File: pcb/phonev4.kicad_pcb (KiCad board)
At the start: 2 copper layers, 88.9 x 124.5 mm, 25 parts, among them J1 coin, J2 keypad, J3 display, J4 RJ9, J5 mic, J6 card_reader, J7 speaker, U2 LM386

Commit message: pcb: Rename power nets 5v→5V_MAIN, 12v→12V_COIN (fixes #69)
- Schematic: global_label and TP1 Value
- PCB: net definitions, pads, pour zone net_name

Co-authored-by: Cursor <cursoragent@cursor.com>
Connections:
- net 12v renamed 12V_COIN
- net 5v renamed 5V_MAIN
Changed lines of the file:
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@@
   (net 0 "")
   (net 1 "unconnected-(A1-3.3V-Pad3V3)")
-  (net 2 "5v")
+  (net 2 "5V_MAIN")
   (net 3 "mag_cls")
   (net 4 "unconnected-(A1-PadAREF)")
@@
   (net 86 "unconnected-(J3-Pin_24-Pad24)")
   (net 87 "gnd")
-  (net 88 "12v")
+  (net 88 "12V_COIN")
   (net 89 "coin_tx")
   (net 90 "coin_rx")
@@
       (net 107 "Net-(C3-Pad1)") (pintype "output") (solder_mask_margin 0.102))
     (pad "6" thru_hole circle (at 1.27 -3.81) (size 1.7272 1.7272) (drill 0.8128) (layers "*.Cu" "*.Mask")
-      (net 88 "12v") (pinfunction "V+") (pintype "power_in") (solder_mask_margin 0.102))
+      (net 88 "12V_COIN") (pinfunction "V+") (pintype "power_in") (solder_mask_margin 0.102))
     (pad "7" thru_hole circle (at -1.27 -3.81) (size 1.7272 1.7272) (drill 0.8128) (layers "*.Cu" "*.Mask")
       (net 106 "Net-(U2-BYPASS)") (pinfunction "BYPASS") (pintype "input") (solder_mask_margin 0.102))
@@
       (net 29 "disp_d7") (pinfunction "Pin_1") (pintype "passive"))
     (pad "2" thru_hole circle (at 2.54 0 90) (size 1.7 1.7) (drill 1) (layers "*.Cu" "*.Mask")
-      (net 2 "5v") (pinfunction "Pin_2") (pintype "passive"))
+      (net 2 "5V_MAIN") (pinfunction "Pin_2") (pintype "passive"))
     (pad "3" thru_hole circle (at 0 2.54 90) (size 1.7 1.7) (drill 1) (layers "*.Cu" "*.Mask")
       (net 28 "disp_d6") (pinfunction "Pin_3") (pintype "passive"))
@@
       (net 87 "gnd") (pinfunction "Pin_8") (pintype "passive"))
     (pad "9" thru_hole circle (at 0 10.16 90) (size 1.7 1.7) (drill 1) (layers "*.Cu" "*.Mask")
-      (net 88 "12v") (pinfunction "Pin_9") (pintype "passive"))
+      (net 88 "12V_COIN") (pinfunction "Pin_9") (pintype "passive"))
     (pad "10" thru_hole circle (at 2.54 10.16 90) (size 1.7 1.7) (drill 1) (layers "*.Cu" "*.Mask")
       (net 91 "coin_reset") (pinfunction "Pin_10") (pintype "passive"))
@@
       (stroke (width 0.1) (type solid)) (layer "F.Fab"))
     (pad "1" thru_hole circle (at 0 0 90) (size 1.6 1.6) (drill 0.8) (layers "*.Cu" "*.Mask")
-      (net 2 "5v") (pintype "passive"))
+      (net 2 "5V_MAIN") (pintype "passive"))
     (pad "2" thru_hole oval (at 7.5 0 90) (size 1.6 1.6) (drill 0.8) (layers "*.Cu" "*.Mask")
       (net 87 "gnd") (pintype "passive"))
@@
       (net 87 "gnd") (pintype "passive"))
     (pad "2" thru_hole oval (at 7.5 0 270) (size 1.6 1.6) (drill 0.8) (layers "*.Cu" "*.Mask")
-      (net 2 "5v") (pintype "passive"))
+      (net 2 "5V_MAIN") (pintype "passive"))
     (model "${KICAD6_3DMODEL_DIR}/Capacitor_THT.3dshapes/C_Axial_L3.8mm_D2.6mm_P7.50mm_Horizontal.wrl"
       (offset (xyz 0 0 0))
@@
       (stroke (width 0.1) (type solid)) (layer "F.Fab"))
     (pad "1" thru_hole circle (at 0 0 180) (size 1.6 1.6) (drill 0.8) (layers "*.Cu" "*.Mask")
-      (net 2 "5v") (pintype "passive"))
+      (net 2 "5V_MAIN") (pintype "passive"))
     (pad "2" thru_hole oval (at 7.5 0 180) (size 1.6 1.6) (drill 0.8) (layers "*.Cu" "*.Mask")
       (net 87 "gnd") (pintype "passive"))
@@
       (stroke (width 0.1) (type solid)) (layer "F.Fab"))
     (pad "1" thru_hole circle (at 0 0 90) (size 1.6 1.6) (drill 0.8) (layers "*.Cu" "*.Mask")
-      (net 88 "12v") (pintype "passive"))
+      (net 88 "12V_COIN") (pintype "passive"))
     (pad "2" thru_hole oval (at 7.5 0 90) (size 1.6 1.6) (drill 0.8) (layers "*.Cu" "*.Mask")
       (net 87 "gnd") (pintype "passive"))
@@
       (net 33 "unconnected-(A3-3V3[1]-Pad1)") (pinfunction "3V3[1]") (pintype "power_in") (solder_mask_margin 0.102))
     (pad "2" thru_hole circle (at -24.13 -1.27 90) (size 1.508 1.508) (drill 1) (layers "*.Cu" "*.Mask")
-      (net 2 "5v") (pinfunction "5V[1]") (pintype "power_in") (solder_mask_margin 0.102))
+      (net 2 "5V_MAIN") (pinfunction "5V[1]") (pintype "power_in") (solder_mask_margin 0.102))
     (pad "3" thru_hole circle (at -21.59 1.27 90) (size 1.508 1.508) (drill 1) (layers "*.Cu" "*.Mask")
       (net 34 "unconnected-(A3-GPIO2{slash}SDA-Pad3)") (pinfunction "GPIO2/SDA") (pintype "bidirectional") (solder_mask_margin 0.102))
     (pad "4" thru_hole circle (at -21.59 -1.27 90) (size 1.508 1.508) (drill 1) (layers "*.Cu" "*.Mask")
-      (net 2 "5v") (pinfunction "5V[2]") (pintype "power_in") (solder_mask_margin 0.102))
+      (net 2 "5V_MAIN") (pinfunction "5V[2]") (pintype "power_in") (solder_mask_margin 0.102))
     (pad "5" thru_hole circle (at -19.05 1.27 90) (size 1.508 1.508) (drill 1) (layers "*.Cu" "*.Mask")
       (net 35 "unconnected-(A3-GPIO3{slash}SCL-Pad5)") (pinfunction "GPIO3/SCL") (pintype "bidirectional") (solder_mask_margin 0.102))
@@
       (net 1 "unconnected-(A1-3.3V-Pad3V3)") (pinfunction "3.3V") (pintype "power_out"))
     (pad "5V" thru_hole oval (at 31.86 -1.38) (size 1.7272 1.7272) (drill 1.016) (layers "*.Cu" "*.Mask")
-      (net 2 "5v") (pinfunction "5V") (pintype "power_in"))
+      (net 2 "5V_MAIN") (pinfunction "5V") (pintype "power_in"))
     (pad "A0" thru_hole oval (at 11.54 -1.38) (size 1.7272 1.7272) (drill 1.016) (layers "*.Cu" "*.Mask")
       (net 93 "key_col_5") (pinfunction "A0") (pintype "bidirectional"))
@@
       (net 12 "ss") (pinfunction "SPI_CS") (pintype "bidirectional"))
     (pad "VIN" thru_hole oval (at 39.48 -1.38) (size 1.7272 1.7272) (drill 1.016) (layers "*.Cu" "*.Mask")
-      (net 2 "5v") (pinfunction "VIN") (pintype "power_in"))
+      (net 2 "5V_MAIN") (pinfunction "VIN") (pintype "power_in"))
   )
   (footprint "Connector_IDC:IDC-Header_2x07_P2.54mm_Vertical" (layer "F.Cu")
@@
       (net 73 "unconnected-(J6-Pin_10-Pad10)") (pinfunction "Pin_10") (pintype "passive"))
     (pad "11" thru_hole circle (at 0 12.7 90) (size 1.7 1.7) (drill 1) (layers "*.Cu" "*.Mask")
-      (net 2 "5v") (pinfunction "Pin_11") (pintype "passive"))
+      (net 2 "5V_MAIN") (pinfunction "Pin_11") (pintype "passive"))
     (pad "12" thru_hole circle (at 2.54 12.7 90) (size 1.7 1.7) (drill 1) (layers "*.Cu" "*.Mask")
       (net 61 "card_seated") (pinfunction "Pin_12") (pintype "passive"))
@@
       (net 13 "unconnected-(A2-3.3V-Pad3V3)") (pinfunction "3.3V") (pintype "power_out"))
     (pad "5V" thru_hole oval (at 31.86 -1.38) (size 1.7272 1.7272) (drill 1.016) (layers "*.Cu" "*.Mask")
-      (net 2 "5v") (pinfunction "5V") (pintype "power_in"))
+      (net 2 "5V_MAIN") (pinfunction "5V") (pintype "power_in"))
     (pad "A0" thru_hole oval (at 11.54 -1.38) (size 1.7272 1.7272) (drill 1.016) (layers "*.Cu" "*.Mask")
       (net 110 "unconnected-(A2-PadA0)") (pinfunction "A0") (pintype "bidirectional"))
@@
       (net 17 "disp_x4") (pinfunction "SPI_CS") (pintype "bidirectional"))
     (pad "VIN" thru_hole oval (at 39.48 -1.38) (size 1.7272 1.7272) (drill 1.016) (layers "*.Cu" "*.Mask")
-      (net 2 "5v") (pinfunction "VIN") (pintype "power_in"))
+      (net 2 "5V_MAIN") (pinfunction "VIN") (pintype "power_in"))
   )
   (footprint "Resistor_THT:R_Axial_DIN0204_L3.6mm_D1.6mm_P7.62mm_Horizontal" (layer "F.Cu")
@@
       (stroke (width 0.1) (type solid)) (layer "F.Fab"))
     (pad "1" thru_hole circle (at 0 0 270) (size 1.4 1.4) (drill 0.7) (layers "*.Cu" "*.Mask")
-      (net 2 "5v") (pintype "passive"))
+      (net 2 "5V_MAIN") (pintype "passive"))
     (pad "2" thru_hole oval (at 7.62 0 270) (size 1.4 1.4) (drill 0.7) (layers "*.Cu" "*.Mask")
       (net 19 "sda") (pintype "passive"))
@@
       (stroke (width 0.1) (type solid)) (layer "F.Fab"))
     (pad "1" thru_hole circle (at 0 0 270) (size 1.4 1.4) (drill 0.7) (layers "*.Cu" "*.Mask")
-      (net 2 "5v") (pintype "passive"))
+      (net 2 "5V_MAIN") (pintype "passive"))
     (pad "2" thru_hole oval (at 7.62 0 270) (size 1.4 1.4) (drill 0.7) (layers "*.Cu" "*.Mask")
       (net 20 "scl") (pintype "passive"))
@@
       (stroke (width 0.1) (type solid)) (layer "F.Fab"))
     (pad "1" thru_hole circle (at 0 0 180) (size 1.6 1.6) (drill 0.8) (layers "*.Cu" "*.Mask")
-      (net 2 "5v") (pintype "passive"))
+      (net 2 "5V_MAIN") (pintype "passive"))
     (pad "2" thru_hole oval (at 7.5 0 180) (size 1.6 1.6) (drill 0.8) (layers "*.Cu" "*.Mask")
       (net 87 "gnd") (pintype "passive"))
@@
       (stroke (width 0.15) (type solid)) (fill none) (layer "F.SilkS"))
     (pad "1" thru_hole rect (at -41.3258 -19.1516 90) (size 1.524 1.524) (drill 1) (layers "*.Cu" "*.Mask" "F.SilkS")
-      (net 2 "5v") (pinfunction "IN+") (pintype "input"))
+      (net 2 "5V_MAIN") (pinfunction "IN+") (pintype "input"))
     (pad "2" thru_hole rect (at -41.3258 -1.9812 90) (size 1.524 1.524) (drill 1) (layers "*.Cu" "*.Mask" "F.SilkS")
       (net 87 "gnd") (pinfunction "IN-") (pintype "input"))
@@
       (net 87 "gnd") (pinfunction "OUT-") (pintype "output"))
     (pad "4" thru_hole rect (at -1.8542 -19.1262 90) (size 1.524 1.524) (drill 1) (layers "*.Cu" "*.Mask" "F.SilkS")
-      (net 88 "12v") (pinfunction "OUT+") (pintype "output"))
+      (net 88 "12V_COIN") (pinfunction "OUT+") (pintype "output"))
   )
   (footprint "Capacitor_THT:CP_Radial_D8.0mm_P3.80mm" (layer "F.Cu")
@@
       (stroke (width 0.1) (type solid)) (fill none) (layer "F.Fab"))
     (pad "1" thru_hole rect (at 0 0) (size 1.6 1.6) (drill 0.8) (layers "*.Cu" "*.Mask")
-      (net 88 "12v") (pintype "passive"))
+      (net 88 "12V_COIN") (pintype "passive"))
     (pad "2" thru_hole circle (at 3.8 0) (size 1.6 1.6) (drill 0.8) (layers "*.Cu" "*.Mask")
       (net 87 "gnd") (pintype "passive"))
@@
     )
   )
-  (zone (net 2) (net_name "5v") (layer "B.Cu") (hatch edge 0.5)
+  (zone (net 2) (net_name "5V_MAIN") (layer "B.Cu") (hatch edge 0.5)
     (priority 1)
     (connect_pads (clearance 0.5))

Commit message: pcb: Move D2 ESD protection from coin_rx to speaker_front+
- D2 (PRTR5V0U2X) now protects speaker_front+ (TDA2822 ringer output)
  instead of coin_rx; coin validator control board isolates serial
- D1 protects mic+ and speaker_receiver+ on J4; D2 I/O2 left unconnected
- Add SCHEMATIC_D2_CHANGES.md with implementation notes and I/O2 options
- Update README, BOM, AUDIT to match

Co-authored-by: Cursor <cursoragent@cursor.com>
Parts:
- added C10: 100nF, Capacitor_THT:C_Axial_L3.8mm_D2.6mm_P7.50mm_Horizontal, F.Cu at (79.6, 55.1)
- added C11: 100µF 16V, Capacitor_THT:CP_Radial_D8.0mm_P3.80mm, F.Cu at (71.4, 49.5)
- added C6: 100nF, Capacitor_THT:C_Axial_L3.8mm_D2.6mm_P7.50mm_Horizontal, F.Cu at (79.6, 46.8)
- added C7: 100µF 16V, Capacitor_THT:CP_Radial_D8.0mm_P3.80mm, F.Cu at (71.4, 59.0)
- added C8: 4.7µF, Capacitor_THT:CP_Radial_D5.0mm_P2.00mm, F.Cu at (91.0, 72.0)
- added C9: 100nF, Capacitor_THT:C_Axial_L3.8mm_D2.6mm_P7.50mm_Horizontal, F.Cu at (79.6, 51.0)
- added D1: PRTR5V0U2X, Package_TO_SOT_SMD:SOT-143, F.Cu at (70.5, 66.2)
- added D2: PRTR5V0U2X, Package_TO_SOT_SMD:SOT-143, F.Cu at (74.7, 66.2)
- added D3: Green LED, LED_THT:LED_D5.0mm, F.Cu at (70.8, 72.2)
- added F1: 1A, Capacitor_THT:CP_Radial_D10.0mm_P5.00mm, F.Cu at (81.6, 63.0)
- added Q1: Si2319CDS, Package_TO_SOT_SMD:SOT-23, F.Cu at (92.3, 59.4)
- added R3: 1kΩ, Resistor_THT:R_Axial_DIN0204_L3.6mm_D1.6mm_P7.62mm_Horizontal, F.Cu at (79.5, 70.3)
- added TP1: 5V_MAIN, TestPoint:TestPoint_Loop_D2.50mm_Drill1.0mm, F.Cu at (66.0, 47.0)
- added TP2: Pi 3.3v out, TestPoint:TestPoint_Loop_D2.50mm_Drill1.0mm, F.Cu at (66.0, 51.7)
- added TP3: Ground, TestPoint:TestPoint_Loop_D2.50mm_Drill1.0mm, F.Cu at (66.0, 56.4)
- added TP4: SDA, TestPoint:TestPoint_Loop_D2.50mm_Drill1.0mm, F.Cu at (66.0, 61.0)
- added TP5: SCL, TestPoint:TestPoint_Loop_D2.50mm_Drill1.0mm, F.Cu at (66.0, 65.7)
- C12: renamed from C3; value CP_Axial_L18.0mm_D10.0mm_P25.00mm -> 100µF 16V; footprint Capacitor_THT:CP_Radial_D10.0mm_P3.80mm -> Capacitor_THT:CP_Radial_D8.0mm_P3.80mm
- R1, R2: value 10k -> 4.7k
- U2: value LM386 -> TDA2822M; footprint LM386:DIP08 -> Package_DIP:DIP-8_W7.62mm
- renumbered C-arduino1 to C1, C-arduino-display1 to C2, C-card1 to C3, C-coin1 to C4, C-raspi1 to C5
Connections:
- A1 pad GND1: gnd -> GND
- A1 pad GND2: gnd -> GND
- A2 pad GND1: gnd -> GND
- A2 pad GND2: gnd -> GND
- A3 pad 1: unconnected-(A3-3V3[1]-Pad1) -> Net-(A3-3V3[1])
- A3 pad 14: gnd -> GND
- A3 pad 20: gnd -> GND
- A3 pad 25: gnd -> GND
- A3 pad 30: gnd -> GND
- A3 pad 34: gnd -> GND
- A3 pad 39: gnd -> GND
- A3 pad 6: gnd -> GND
- A3 pad 9: gnd -> GND
- C1 pad 2: gnd -> GND
- C12 pad 2: speaker_front+ -> speaker_receiver+
- C2 pad 2: gnd -> GND
- C3 pad 1: gnd -> GND
- C4 pad 2: gnd -> GND
- C5 pad 2: gnd -> GND
- J1 pad 1: gnd -> GND
- J1 pad 4: gnd -> GND
- J1 pad 5: gnd -> GND
- J1 pad 6: gnd -> GND
- J1 pad 7: gnd -> GND
- J1 pad 8: gnd -> GND
- J2 pad 20: gnd -> GND
- J3 pad 26: gnd -> GND
- J4 pad 3: gnd -> GND
- J4 pad 4: gnd -> GND
- J5 pad 2: gnd -> GND
- J6 pad 12: card_seated -> mag_cls
- J6 pad 2: gnd -> GND
- J7 pad 1: speaker_receiver+ -> speaker_receiver_pre+
- J7 pad 2: gnd -> GND
- U1 pad 1: 5V_MAIN -> BOOST_IN+
- U1 pad 2: gnd -> GND
- U1 pad 3: gnd -> GND
- U2 pad 1: unconnected-(U2-GAIN-Pad1) -> Net-(U2-OUT_A)
- U2 pad 2: gnd -> GND
- U2 pad 3: speaker_front_pre+ -> Net-(U2-IN_A)
- U2 pad 4: gnd -> Net-(U2-IN_B)
- U2 pad 6: 12V_COIN -> 5V_MAIN
- U2 pad 7: Net-(U2-BYPASS) -> Net-(U2-RIPPLE)
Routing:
- net 12V_COIN: track 170.7 -> 38.7 mm
- net speaker_front+: track 118.6 -> 0.00 mm
- net gnd: track 111.4 -> 0.00 mm, vias 2 -> 0
- net GND: track 0.00 -> 95.4 mm, vias 0 -> 2
- net speaker_front_pre+: track 48.1 -> 0.00 mm
- net Net-(U2-OUT_B): track 23.7 -> 0.00 mm
- net speaker_receiver+: track 19.6 -> 0.00 mm
- net Net-(U2-BYPASS): track 16.1 -> 0.00 mm
- added copper zone on F.Cu, net GND
- removed copper zone on F.Cu, net gnd

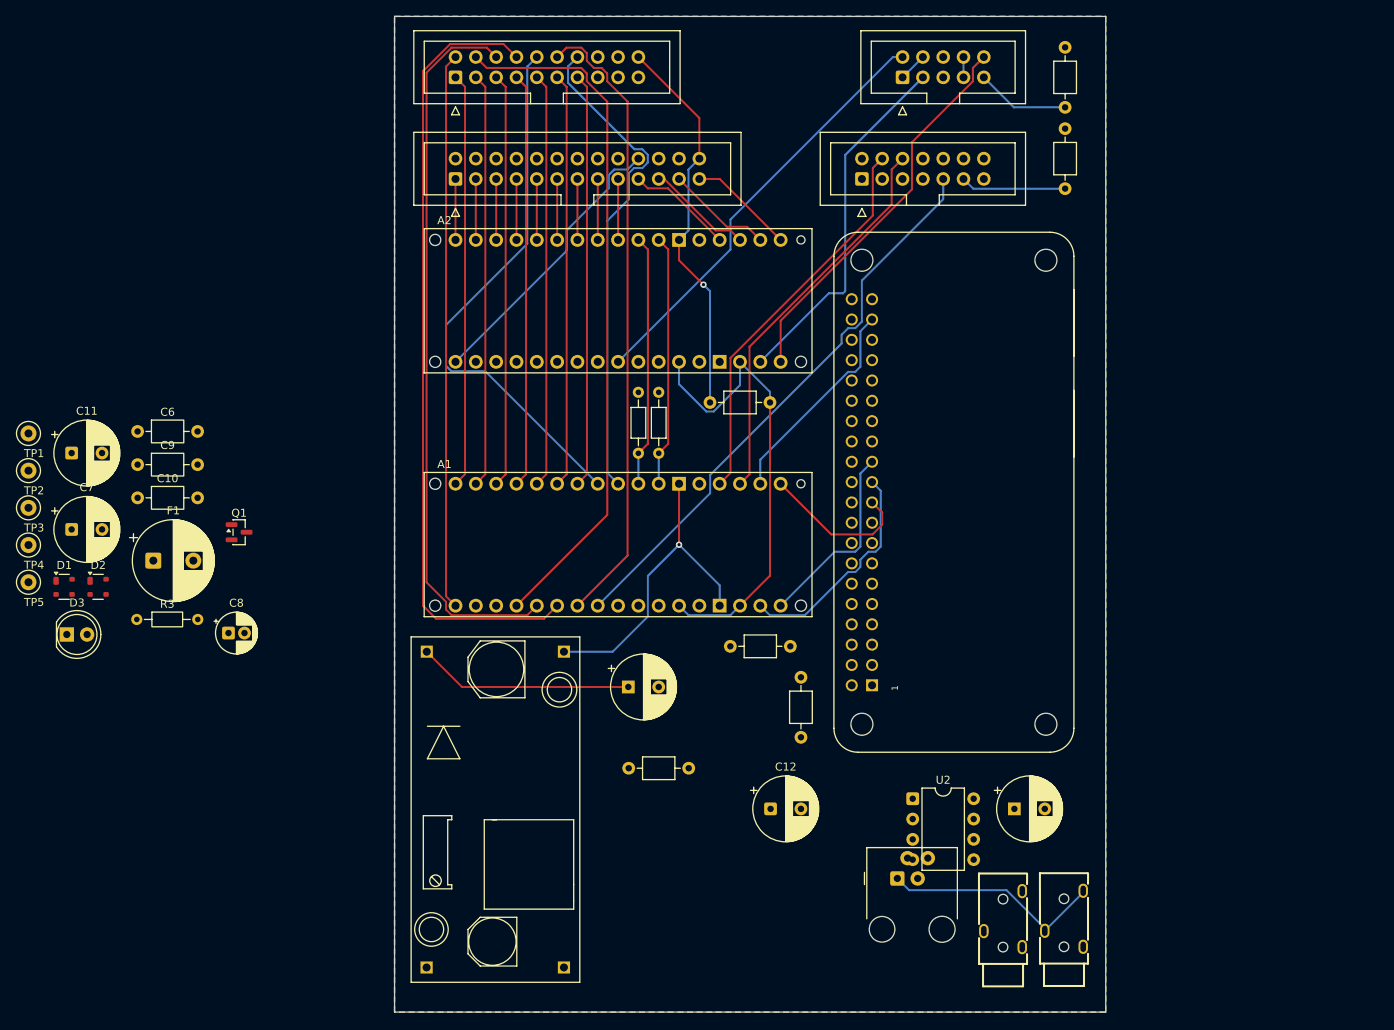
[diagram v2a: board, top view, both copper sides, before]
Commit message: pcb: diode reannotation, ERC fixes, no-connect markers
- Update docs for D1-D3 (P6KE6.8CA TVS), D4 (power LED)
- Add PWR_FLAGs for 5V_MAIN, GND, 3.3V nets
- Fix C6/C7 bypass wiring (parallel to GND, not series)
- Add no_connect markers for 59 intentionally unused pins
- Remove dangling wires at 288.29mm and 110.49/130.81
- Add add_no_connect.py script for future ERC sync
- Add F1 fuse footprint, fp-lib-table, DESIGN_OPTIONS

Co-authored-by: Cursor <cursoragent@cursor.com>
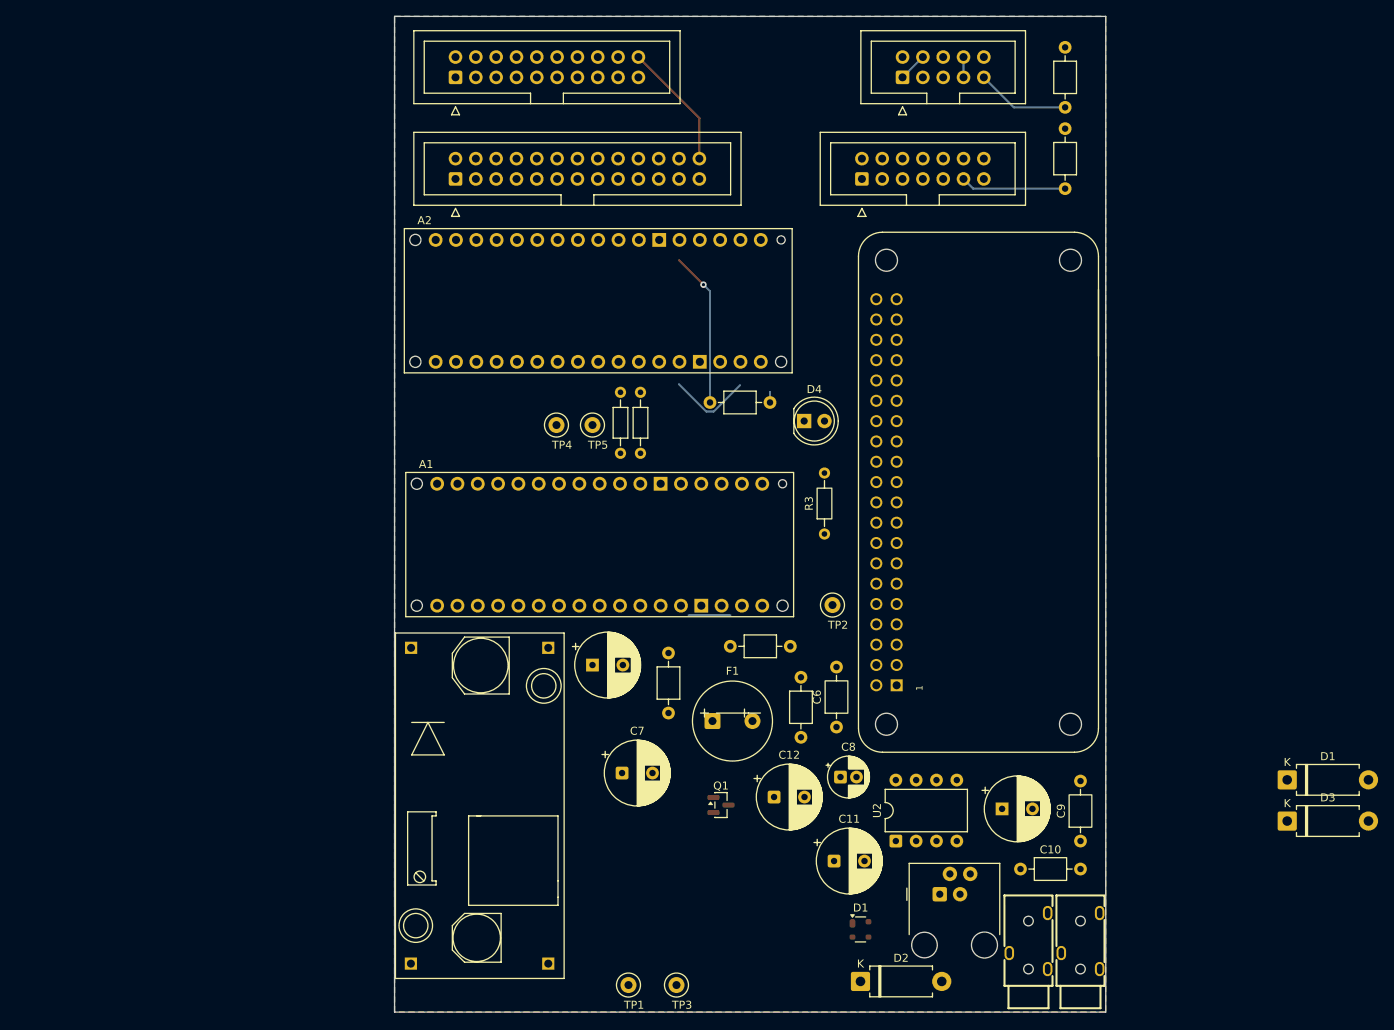
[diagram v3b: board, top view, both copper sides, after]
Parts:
- added D1: P6KE6.8CA, Diode_THT:D_DO-15_P10.16mm_Horizontal, F.Cu at (223.3, 90.3)
- added D3: P6KE6.8CA, Diode_THT:D_DO-15_P10.16mm_Horizontal, F.Cu at (223.3, 95.5)
- D2: value PRTR5V0U2X -> P6KE6.8CA; footprint Package_TO_SOT_SMD:SOT-143 -> Diode_THT:D_DO-15_P10.16mm_Horizontal
- F1: footprint Capacitor_THT:CP_Radial_D10.0mm_P5.00mm -> footprints:Fuse_Radial_D10.0mm_P5.00mm
- moved C9 126.9 mm to (197.5, 98.0), turned to 90 degrees
- moved C10 119.7 mm to (190.0, 101.5)
- moved D1 108.4 mm to (170.0, 109.0)
- moved C11 108.1 mm to (166.7, 100.5)
- moved D2 107.3 mm to (170.0, 115.5)
- moved TP2 101.9 mm to (166.5, 68.5)
- moved TP1 101.9 mm to (141.0, 116.0)
- moved TP3 100.6 mm to (147.0, 116.0)
- moved D4 96.0 mm to (163.0, 45.5)
- moved C6 94.9 mm to (167.0, 83.8), turned to 90 degrees
- moved R3 86.6 mm to (165.5, 59.6), turned to 90 degrees
- moved C8 78.6 mm to (167.5, 90.0)
- moved C7 75.2 mm to (140.2, 89.5)
- moved TP5 73.2 mm to (136.5, 46.0)
- moved F1 72.7 mm to (151.5, 83.0)
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- renumbered D3 to D4
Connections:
- C6 pad 2: 5V_MAIN -> Net-(U2-V+)
- C7 pad 2: 5V_MAIN -> Net-(U2-V+)
- D2 pad 1: GND -> speaker_front+
- D2 pad 2: speaker_front+ -> GND
- U2 pad 6: 5V_MAIN -> Net-(U2-V+)
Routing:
- net key_col_7: track 98.7 -> 0.00 mm
- net key_col_6: track 90.7 -> 0.00 mm
- net key_col_5: track 87.0 -> 0.00 mm
- net key_hook_common: track 78.8 -> 0.00 mm
- net mag_cls: track 71.7 -> 0.00 mm
- net key_col_4: track 69.6 -> 0.00 mm
- net key_hook_up: track 68.4 -> 0.00 mm
- net key_hook_down: track 61.8 -> 0.00 mm
- net GND: track 95.4 -> 41.4 mm, vias 2 -> 1
- net coin_tx: track 53.5 -> 0.00 mm
- net key_row_4: track 51.8 -> 0.00 mm
- net key_row_2: track 51.8 -> 0.00 mm
- net key_row_1: track 51.8 -> 0.00 mm
- net key_col_3: track 51.8 -> 0.00 mm
- net key_col_1: track 51.8 -> 0.00 mm
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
